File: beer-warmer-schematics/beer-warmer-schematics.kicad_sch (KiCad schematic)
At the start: 32 parts, among them J1 USB_C_Receptacle_USB2.0_14P, J2 Screw_Terminal_01x02, J3 Conn_01x07_Socket, J4 Conn_01x07_Socket, J5 Conn_01x04_Pin, J6 Screw_Terminal_01x03, Q1 AOD4184A, U2 LM2596S-5, U3 CH224K

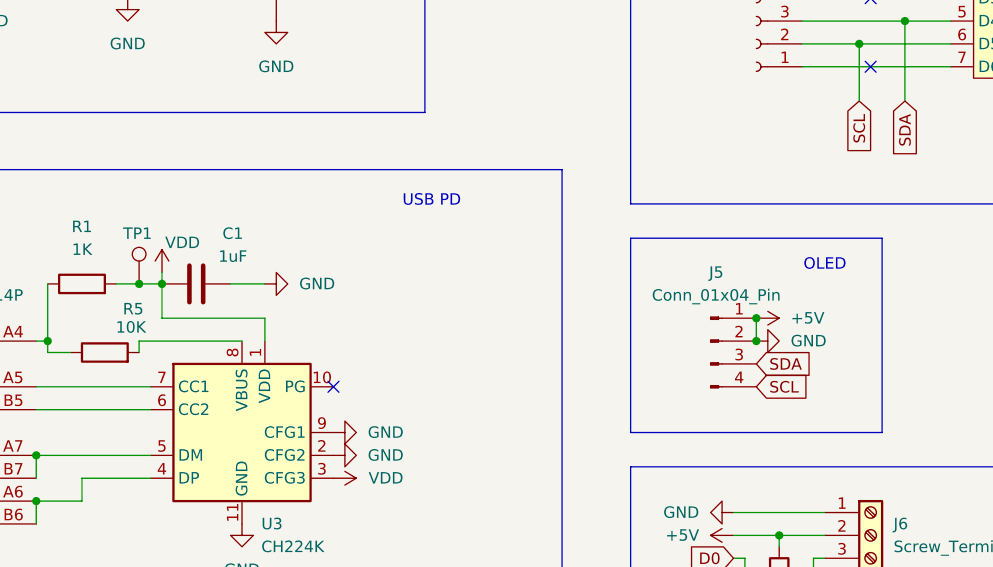
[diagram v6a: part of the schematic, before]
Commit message: imperial footprint sizes
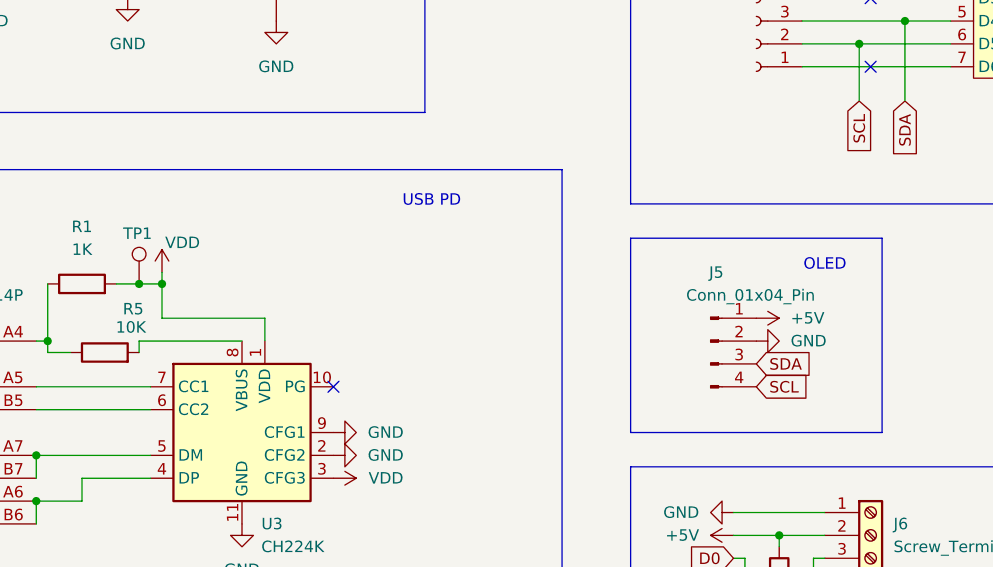
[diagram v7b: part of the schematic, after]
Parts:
- removed C1: 1uF, Capacitor_SMD:CP_Elec_10x10.5, symbol Device:C
- D2, D3: footprint Resistor_SMD:R_0201_0603Metric -> LED_SMD:LED_0603_1608Metric
- R1: footprint Resistor_SMD:R_1206_3216Metric -> Resistor_SMD:R_0402_1005Metric; LCSC C4410 -> C11702
- R2, R4, R5: footprint Resistor_SMD:R_1206_3216Metric -> Resistor_SMD:R_0603_1608Metric; LCSC C17902 -> C15401
- R3, R6: footprint Resistor_SMD:R_0201_0603Metric -> Resistor_SMD:R_0603_1608Metric
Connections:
- net +5V: no longer C2.2, C3.2, D1.2 (A), D2.1 (K), D3.1 (K), J1.A1 (GND), J1.A12 (GND), J1.B1 (GND), J1.B12 (GND), J1.S1 (SHIELD), J3.2 (Pin_2), J5.2 (Pin_2), J6.1 (Pin_1), Q1.2 (D), R2.2, U1.13 (GND), U2.3 (GND), U2.5 (~{ON}/OFF), U3.11 (GND), U3.2 (CFG2), U3.9 (CFG1)
- new net GND: C2.2, C3.2, D1.2 (A), D2.1 (K), D3.1 (K), J1.A1 (GND), J1.A12 (GND), J1.B1 (GND), J1.B12 (GND), J1.S1 (SHIELD), J3.2 (Pin_2), J5.2 (Pin_2), J6.1 (Pin_1), Q1.2 (D), R2.2, U1.13 (GND), U2.3 (GND), U2.5 (~{ON}/OFF), U3.11 (GND), U3.2 (CFG2), U3.9 (CFG1)
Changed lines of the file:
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@@
 	)
 	(junction
-		(at 146.05 78.74)
-		(diameter 0)
-		(color 0 0 0 0)
-	)
-	(junction
 		(at 157.48 35.56)
 		(diameter 0)
@@
 	)
 	(junction
-		(at 146.05 81.28)
-		(diameter 0)
-		(color 0 0 0 0)
-	)
-	(junction
 		(at 199.39 35.56)
 		(diameter 0)
@@
 	(wire
 		(pts
-			(xy 146.05 78.74) (xy 146.05 81.28)
-		)
-		(stroke
-			(width 0)
-			(type default)
-		)
-	)
-	(wire
-		(pts
 			(xy 73.66 30.48) (xy 92.71 30.48)
 		)
@@
 	(wire
 		(pts
-			(xy 87.63 74.93) (xy 91.44 74.93)
-		)
-		(stroke
-			(width 0)
-			(type default)
-		)
-	)
-	(wire
-		(pts
 			(xy 77.47 81.28) (xy 77.47 82.55)
 		)
@@
 			)
 		)
-		(property "Footprint" "Resistor_SMD:R_1206_3216Metric"
+		(property "Footprint" "Resistor_SMD:R_0603_1608Metric"
 			(at 73.66 84.328 90)
 			(effects
@@
 			)
 		)
-		(property "LCSC" "C17902"
+		(property "LCSC" "C15401"
 			(at 73.66 82.55 90)
 			(effects
@@
 			)
 		)
-		(property "Footprint" "Resistor_SMD:R_1206_3216Metric"
+		(property "Footprint" "Resistor_SMD:R_0603_1608Metric"
 			(at 50.8 165.862 90)
 			(effects
@@
 			)
 		)
-		(property "LCSC" "C17902"
+		(property "LCSC" "C15401"
 			(at 50.8 167.64 90)
 			(effects
@@
 			)
 		)
-		(property "Footprint" "Resistor_SMD:R_0201_0603Metric"
+		(property "Footprint" "Resistor_SMD:R_0603_1608Metric"
 			(at 219.71 58.928 90)
 			(effects
@@
 			)
 		)
-		(property "Footprint" "Resistor_SMD:R_0201_0603Metric"
+		(property "Footprint" "Resistor_SMD:R_0603_1608Metric"
 			(at 50.8 155.702 90)
 			(effects
@@
 			)
 		)
-		(property "Footprint" "Resistor_SMD:R_0201_0603Metric"
+		(property "Footprint" "LED_SMD:LED_0603_1608Metric"
 			(at 227.33 57.15 0)
 			(effects
@@
 	)
 	(symbol
-		(lib_id "Device:C")
-		(at 83.82 74.93 90)
-		(unit 1)
-		(exclude_from_sim no)
-		(in_bom yes)
-		(on_board yes)
-		(dnp no)
-		(property "Reference" "C1"
-			(at 87.884 69.342 90)
-			(effects
-				(font
-					(size 1.27 1.27)
-				)
-			)
-		)
-		(property "Value" "1uF"
-			(at 87.884 71.882 90)
-			(effects
-				(font
-					(size 1.27 1.27)
-				)
-			)
-		)
-		(property "Footprint" "Capacitor_SMD:CP_Elec_10x10.5"
-			(at 87.63 73.9648 0)
-			(effects
-				(font
-					(size 1.27 1.27)
-				)
-				(hide yes)
-			)
-		)
-		(property "Datasheet" "~"
-			(at 83.82 74.93 0)
-			(effects
-				(font
-					(size 1.27 1.27)
-				)
-				(hide yes)
-			)
-		)
-		(property "Description" "Unpolarized capacitor"
-			(at 83.82 74.93 0)
-			(effects
-				(font
-					(size 1.27 1.27)
-				)
-				(hide yes)
-			)
-		)
-		(property "LCSC" "C7471898"
-			(at 83.82 74.93 90)
-			(effects
-				(font
-					(size 1.27 1.27)
-				)
-				(hide yes)
-			)
-		)
-		(pin "1"
-		)
-		(pin "2"
-		)
-		(instances
-			(project ""
-				(path "/70572ac2-8723-48b8-abb1-12d225a3bb68"
-					(reference "C1")
-					(unit 1)
-				)
-			)
-		)
-	)
-	(symbol
 		(lib_id "Mechanical:Fiducial")
 		(at 208.28 80.01 0)
@@
 	)
 	(symbol
-		(lib_id "power:GND")
-		(at 46.99 167.64 270)
-		(unit 1)
-		(exclude_from_sim no)
-		(in_bom yes)
-		(on_board yes)
-		(dnp no)
-		(fields_autoplaced yes)
-		(property "Reference" "#PWR020"
-			(at 40.64 167.64 0)
-			(effects
-				(font
-					(size 1.27 1.27)
-				)
-				(hide yes)
-			)
-		)
-		(property "Value" "GND"
-			(at 43.18 167.6399 90)
-			(effects
-				(font
-					(size 1.27 1.27)
-				)
-				(justify right)
-			)
-		)
-		(property "Footprint" ""
-			(at 46.99 167.64 0)
-			(effects
-				(font
-					(size 1.27 1.27)
-				)
-				(hide yes)
-			)
-		)
-		(property "Datasheet" ""
-			(at 46.99 167.64 0)
-			(effects
-				(font
-					(size 1.27 1.27)
-				)
-				(hide yes)
-			)
-		)
-		(property "Description" "Power symbol creates a global label with name \"GND\" , ground"
-			(at 46.99 167.64 0)
-			(effects
-				(font
-					(size 1.27 1.27)
-				)
-				(hide yes)
-			)
-		)
-		(pin "1"
-		)
-		(instances
-			(project ""
-				(path "/70572ac2-8723-48b8-abb1-12d225a3bb68"
-					(reference "#PWR020")
-					(unit 1)
-				)
-			)
-		)
-	)
-	(symbol
 		(lib_id "New_Library:Seed_Studio_Xiao_ESP32C6")
 		(at 180.34 43.18 0)
@@
 			)
 		)
-		(property "Footprint" "Resistor_SMD:R_1206_3216Metric"
+		(property "Footprint" "Resistor_SMD:R_0402_1005Metric"
 			(at 71.12 76.708 90)
 			(effects
@@
 			)
 		)
-		(property "LCSC" "C4410"
+		(property "LCSC" "C11702"
 			(at 71.12 74.93 90)
 			(effects
@@
 		(on_board yes)
 		(dnp no)
-		(fields_autoplaced yes)
 		(property "Reference" "J5"
 			(at 141.605 73.66 0)
@@
 		)
 		(property "Value" "Conn_01x04_Pin"
-			(at 141.605 76.2 0)
+			(at 145.415 76.2 0)
 			(effects
 				(font
@@
 			)
 		)
-		(property "Footprint" "Resistor_SMD:R_0201_0603Metric"
+		(property "Footprint" "LED_SMD:LED_0603_1608Metric"
 			(at 43.18 157.48 0)
 			(effects
@@
 			)
 		)
-		(property "Footprint" "Resistor_SMD:R_1206_3216Metric"
+		(property "Footprint" "Resistor_SMD:R_0603_1608Metric"
 			(at 146.812 107.95 90)
 			(effects
@@
 			)
 		)
-		(property "LCSC" "C17902"
+		(property "LCSC" "C15401"
 			(at 148.59 107.95 90)
 			(effects
@@
 	(symbol
 		(lib_id "power:GND")
-		(at 91.44 74.93 90)
+		(at 231.14 57.15 90)
 		(unit 1)
 		(exclude_from_sim no)
@@
 		(dnp no)
 		(fields_autoplaced yes)
-		(property "Reference" "#PWR07"
-			(at 97.79 74.93 0)
+		(property "Reference" "#PWR026"
+			(at 237.49 57.15 0)
 			(effects
 				(font
@@
 		)
 		(property "Value" "GND"
-			(at 95.25 74.9299 90)
+			(at 234.95 57.1501 90)
 			(effects
 				(font
@@
 		)
 		(property "Footprint" ""
-			(at 91.44 74.93 0)
+			(at 231.14 57.15 0)
 			(effects
 				(font
@@
 		)
 		(property "Datasheet" ""
-			(at 91.44 74.93 0)
+			(at 231.14 57.15 0)
 			(effects
 				(font
@@
 		)
 		(property "Description" "Power symbol creates a global label with name \"GND\" , ground"
-			(at 91.44 74.93 0)
+			(at 231.14 57.15 0)
 			(effects
 				(font
@@
 		)
 		(instances
-			(project ""
+			(project "beer-warmer-schematics"
 				(path "/70572ac2-8723-48b8-abb1-12d225a3bb68"
-					(reference "#PWR07")
+					(reference "#PWR026")
 					(unit 1)
 				)
@@
 	(symbol
 		(lib_id "power:GND")
-		(at 231.14 57.15 90)
+		(at 46.99 167.64 270)
 		(unit 1)
 		(exclude_from_sim no)
@@
 		(dnp no)
 		(fields_autoplaced yes)
-		(property "Reference" "#PWR026"
-			(at 237.49 57.15 0)
+		(property "Reference" "#PWR07"
+			(at 40.64 167.64 0)
 			(effects
 				(font
@@
 		)
 		(property "Value" "GND"
-			(at 234.95 57.1501 90)
+			(at 43.18 167.6399 90)
 			(effects
 				(font
@@
 		)
 		(property "Footprint" ""
-			(at 231.14 57.15 0)
+			(at 46.99 167.64 0)
 			(effects
 				(font
@@
 		)
 		(property "Datasheet" ""
-			(at 231.14 57.15 0)
+			(at 46.99 167.64 0)
 			(effects
 				(font
@@
 		)
 		(property "Description" "Power symbol creates a global label with name \"GND\" , ground"
-			(at 231.14 57.15 0)
+			(at 46.99 167.64 0)
 			(effects
 				(font
@@
 		)
 		(instances
-			(project "beer-warmer-schematics"
+			(project ""
 				(path "/70572ac2-8723-48b8-abb1-12d225a3bb68"
-					(reference "#PWR026")
+					(reference "#PWR07")
 					(unit 1)
 				)

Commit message: beefier resistor
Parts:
- R1: footprint Resistor_SMD:R_0402_1005Metric -> Resistor_SMD:R_1206_3216Metric; LCSC C11702 -> C4410
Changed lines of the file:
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@@
 			)
 		)
-		(property "Footprint" "Resistor_SMD:R_0402_1005Metric"
+		(property "Footprint" "Resistor_SMD:R_1206_3216Metric"
 			(at 71.12 76.708 90)
 			(effects
@@
 			)
 		)
-		(property "LCSC" "C11702"
+		(property "LCSC" "C4410"
 			(at 71.12 74.93 90)
 			(effects
